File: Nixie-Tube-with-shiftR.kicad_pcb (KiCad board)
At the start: 2 copper layers, 37 x 44 mm, 55 parts, among them J1 Conn_01x06_Male, J2 Conn_01x01_Female, J3 Conn_01x06_Female, J4 Conn_01x01_Male, Q1 MMBTA42LT1, Q10 MMBTA42LT1, Q11 AO3400, Q12 AO3400, Q13 AO3400, Q14 MMBTA42LT1, Q15 MMBTA42LT1, Q2 MMBTA42LT1, Q3 MMBTA42LT1, Q4 MMBTA42LT1, Q5 MMBTA42LT1, Q6 MMBTA42LT1, Q7 MMBTA42LT1, Q8 MMBTA42LT1, Q9 MMBTA42LT1, U1 74HC595D, U2 nixie-tube, U3 74HC595D, U4 ams1117-5.0

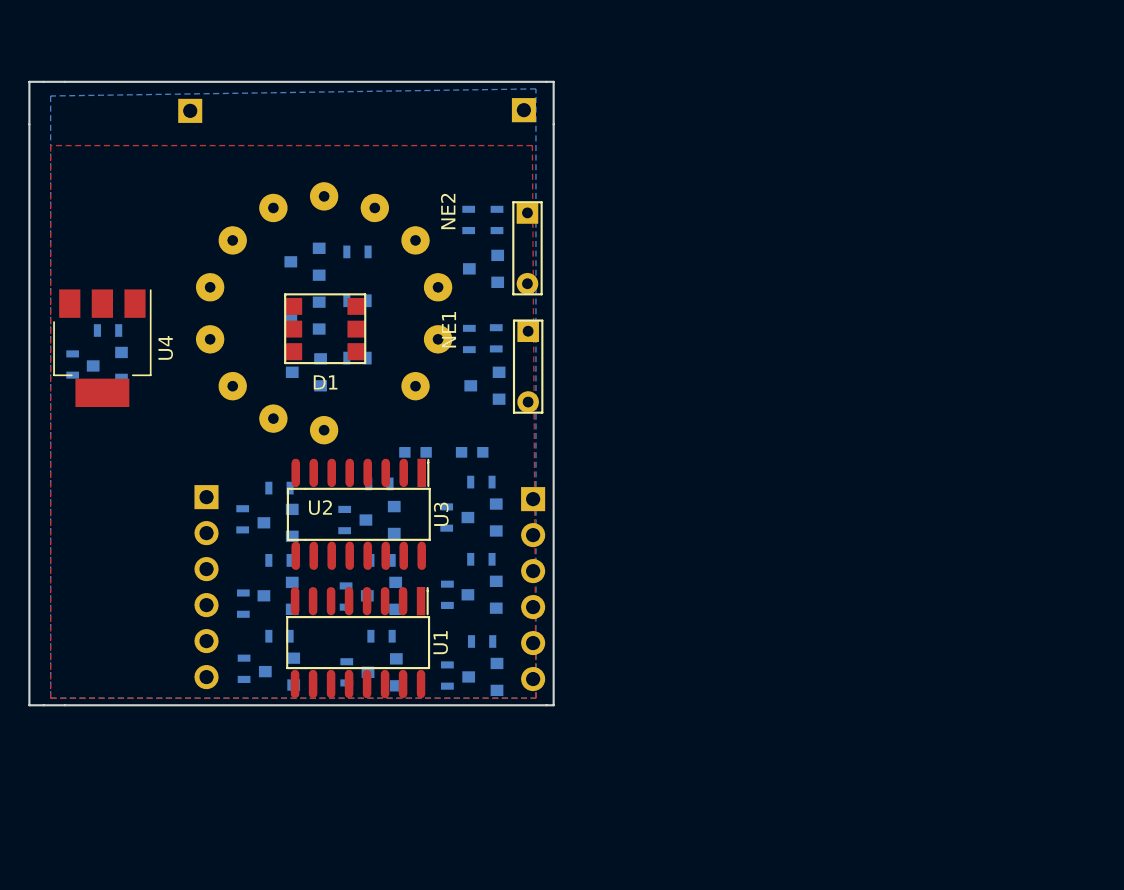
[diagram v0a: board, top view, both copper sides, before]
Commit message: finalized position, briefly routed
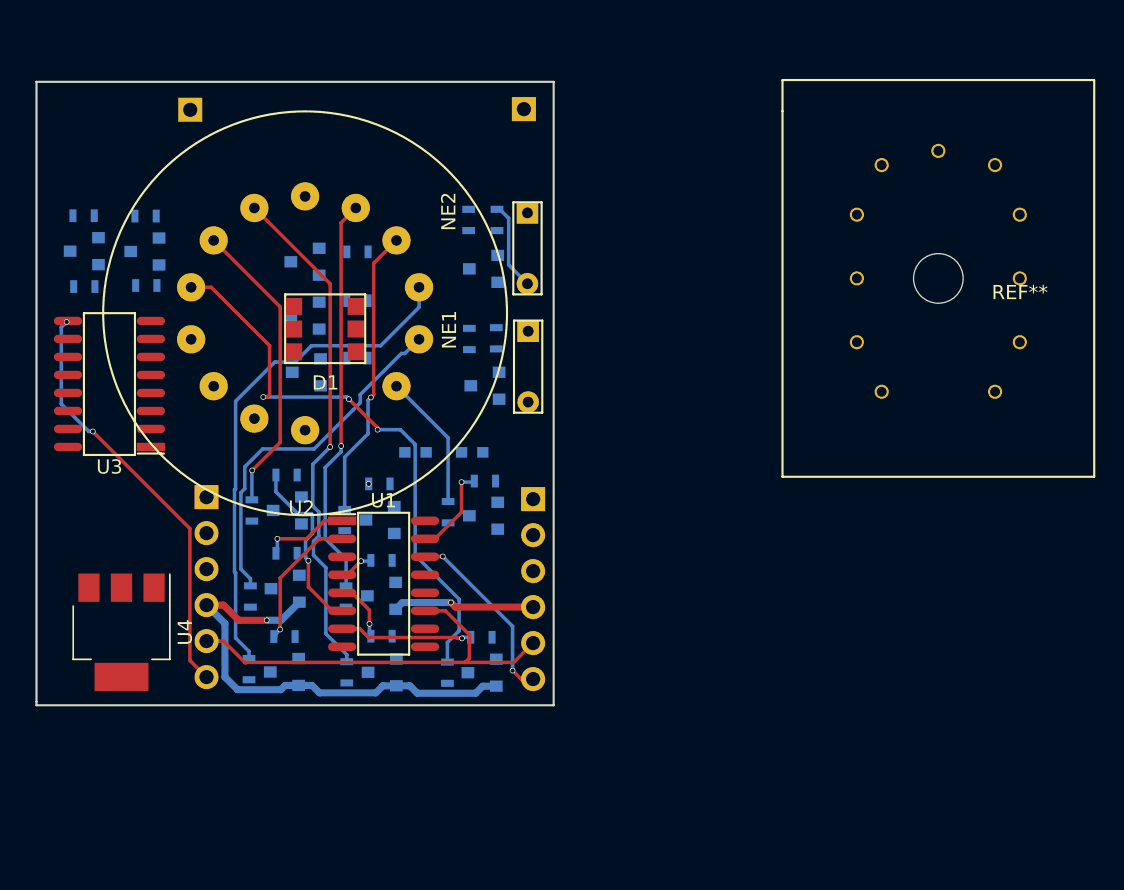
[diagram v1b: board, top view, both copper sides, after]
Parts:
- added REF**: qs27-1, nixie-tube-fp:qs27-1, F.Cu at (215.7, 57.9)
- moved Q3 41.2 mm to (155.4, 56.0)
- moved R16 41.2 mm to (155.3, 53.5)
- moved R2 37.6 mm to (155.4, 58.5), turned to 180 degrees
- moved U4 20.1 mm to (158.0, 82.8)
- moved U3 19.9 mm to (157.2, 65.3), turned to 180 degrees
- moved Q9 14.5 mm to (183.6, 74.6)
- moved R10 14.5 mm to (181.1, 74.4)
- moved R22 14.5 mm to (183.7, 72.2)
- moved Q8 13.8 mm to (169.7, 74.2)
- moved R21 13.8 mm to (169.7, 71.8)
- moved R4 13.8 mm to (167.2, 74.2), turned to 270 degrees
- moved Q1 8.50 mm to (159.7, 56.0)
- moved R14 8.50 mm to (159.7, 53.5)
- moved R1 7.62 mm to (159.8, 58.4), turned to 180 degrees
- moved Q6 5.50 mm to (183.4, 85.7)
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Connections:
- R11 pad 1: +9V -> +5V
- R12 pad 1: +9V -> +5V
- R13 pad 1: +9V -> +5V
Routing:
- net GND: track 0.00 -> 43.7 mm, vias 0 -> 2
- net Net-(R3-Pad1): track 0.00 -> 40.4 mm, vias 0 -> 3
- net Net-(R5-Pad1): track 0.00 -> 36.0 mm, vias 0 -> 1
- net Net-(R8-Pad1): track 0.00 -> 35.7 mm
- net /SCK: track 0.00 -> 30.2 mm
- net /MOSI-OUT: track 0.00 -> 29.7 mm, vias 0 -> 2
- net Net-(R6-Pad1): track 0.00 -> 28.2 mm, vias 0 -> 1
- net Net-(R9-Pad1): track 0.00 -> 25.2 mm
- net Net-(R4-Pad1): track 0.00 -> 21.1 mm, vias 0 -> 1
- net Net-(R7-Pad1): track 0.00 -> 20.5 mm, vias 0 -> 1
- net /MOSI: track 0.00 -> 13.0 mm, vias 0 -> 2
- net /s6: track 0.00 -> 12.9 mm, vias 0 -> 1
- net /s2: track 0.00 -> 9.75 mm, vias 0 -> 1
- net Net-(R10-Pad1): track 0.00 -> 9.65 mm
- net /s7: track 0.00 -> 9.39 mm, vias 0 -> 1
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- removed copper zone on F.Cu, net +9V
- removed copper zone on B.Cu, net GND
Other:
- board size 37 x 44 mm -> 36.5 x 44 mm

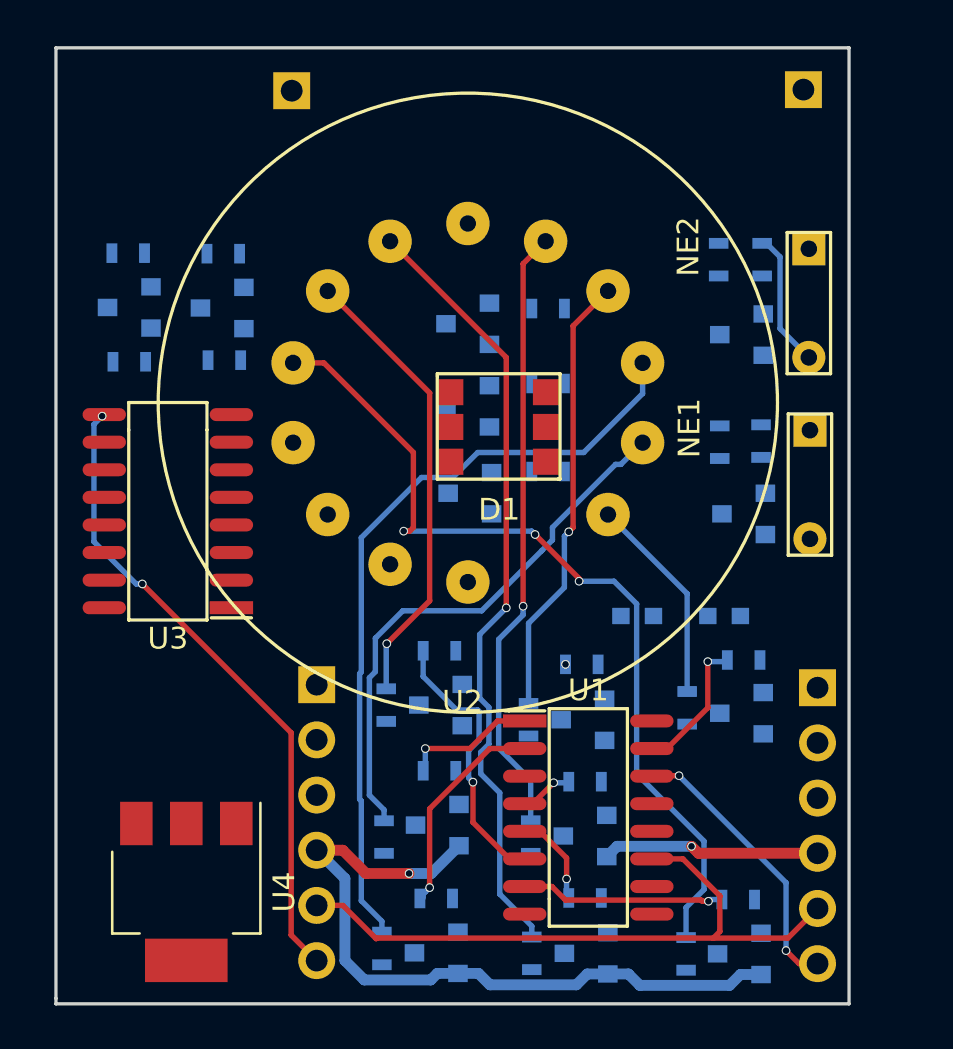
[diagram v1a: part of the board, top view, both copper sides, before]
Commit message: align the components
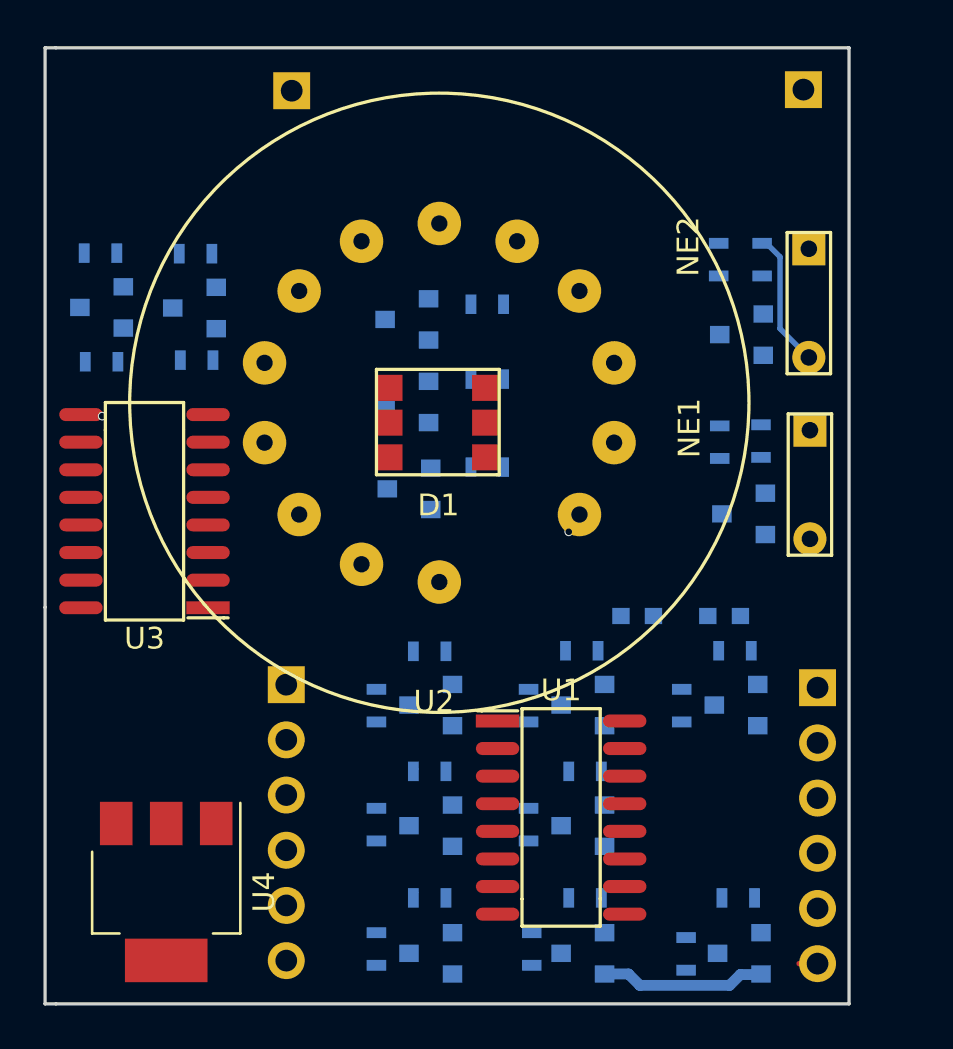
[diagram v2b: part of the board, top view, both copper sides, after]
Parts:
- moved Q11 2.81 mm to (168.2, 64.3)
- moved R11 2.81 mm to (171.8, 63.3)
- moved R12 2.81 mm to (171.8, 59.2)
- moved R13 2.81 mm to (171.8, 55.8)
- moved D1 2.81 mm to (169.7, 61.2)
- moved Q12 2.81 mm to (168.2, 60.3)
- moved Q13 2.81 mm to (168.2, 56.5)
- moved J1 1.40 mm to (162.6, 73.3)
- moved U2 1.31 mm to (169.6, 60.3)
- moved Q1 1.28 mm to (158.4, 56.0)
- moved Q3 1.28 mm to (154.1, 56.0)
- moved R1 1.28 mm to (158.5, 58.4)
- moved R2 1.28 mm to (154.1, 58.5)
- moved R14 1.27 mm to (158.4, 53.5)
- moved R16 1.27 mm to (154.1, 53.5)
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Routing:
- net Net-(R3-Pad1): track 40.4 -> 0.00 mm, vias 3 -> 0
- net GND: track 43.7 -> 7.47 mm, vias 2 -> 0
- net Net-(R5-Pad1): track 36.0 -> 0.00 mm, vias 1 -> 0
- net Net-(R8-Pad1): track 35.7 -> 0.00 mm
- net /SCK: track 30.2 -> 0.00 mm
- net /MOSI-OUT: track 29.7 -> 0.07 mm, vias 2 -> 1
- net Net-(R6-Pad1): track 28.2 -> 0.68 mm, vias 1 -> 0
- net Net-(R9-Pad1): track 25.2 -> 0.00 mm
- net Net-(R4-Pad1): track 21.1 -> 0.00 mm, vias 1 -> 0
- net Net-(R7-Pad1): track 20.5 -> 0.00 mm, vias 1 -> 0
- net /s6: track 12.9 -> 0.00 mm, vias 1 -> 0
- net /MOSI: track 13.0 -> 0.85 mm, vias 2 -> 0
- net /s2: track 9.75 -> 0.32 mm, vias 1 -> 0
- net /s7: track 9.39 -> 0.00 mm, vias 1 -> 0
- net Net-(R10-Pad1): track 9.65 -> 0.28 mm, vias 0 -> 1
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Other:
- board size 36.5 x 44 mm -> 37 x 44 mm

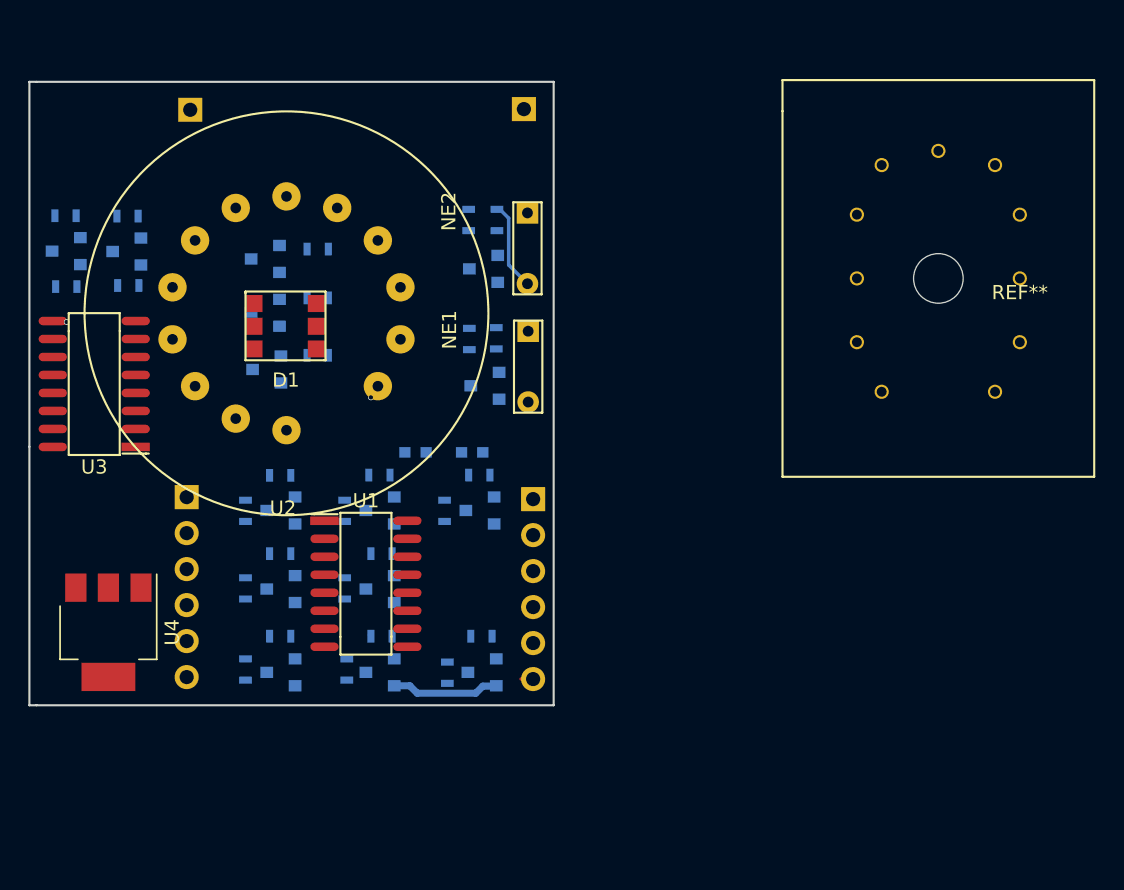
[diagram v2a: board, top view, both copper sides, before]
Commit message: finished routed all tracks
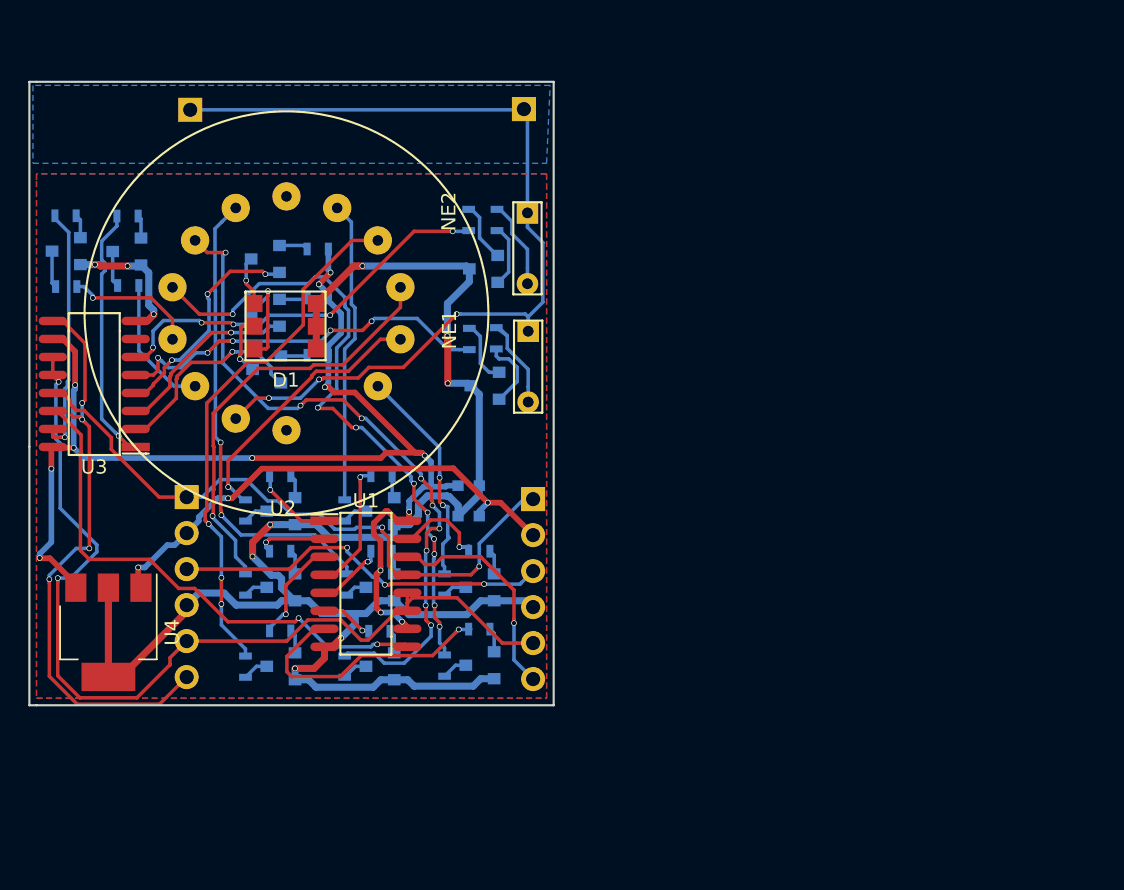
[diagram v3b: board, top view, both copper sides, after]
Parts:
- removed REF**: qs27-1, nixie-tube-fp:qs27-1
- moved Q4 13.0 mm to (169.2, 85.2)
- moved Q8 13.0 mm to (176.2, 85.2)
- moved R17 13.0 mm to (169.2, 82.8)
- moved R21 13.0 mm to (176.2, 82.8)
- moved R4 13.0 mm to (173.8, 85.3)
- moved R7 13.0 mm to (166.8, 85.3)
- moved Q10 6.00 mm to (176.2, 79.7)
- moved Q5 6.00 mm to (169.2, 79.7)
- moved R18 6.00 mm to (169.2, 77.1)
- moved R23 6.00 mm to (176.3, 77.1)
- moved R5 6.00 mm to (173.9, 79.5)
- moved R8 6.00 mm to (166.8, 79.5)
- moved Q2 5.50 mm to (176.2, 74.3)
- moved Q7 5.50 mm to (169.2, 74.3)
- moved R15 5.50 mm to (176.3, 71.8)
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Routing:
- net GND: track 7.47 -> 133.3 mm, vias 0 -> 10
- net +5V: track 0.00 -> 87.3 mm, vias 0 -> 13
- net /SCK: track 0.00 -> 67.1 mm, vias 0 -> 2
- net Net-(J2-Pad1): track 0.00 -> 64.0 mm, vias 0 -> 3
- net Net-(R4-Pad1): track 0.00 -> 48.3 mm, vias 0 -> 9
- net Net-(R3-Pad1): track 0.00 -> 45.8 mm, vias 0 -> 9
- net Net-(J1-Pad1): track 0.00 -> 45.5 mm, vias 0 -> 2
- net /MOSI-OUT: track 0.07 -> 40.7 mm, vias 1 -> 4
- net Net-(R7-Pad1): track 0.00 -> 37.4 mm, vias 0 -> 3
- net Net-(U1-Pad9): track 0.00 -> 37.1 mm, vias 0 -> 2
- net +9V: track 0.00 -> 35.6 mm, vias 0 -> 3
- net Net-(R5-Pad1): track 0.00 -> 33.3 mm, vias 0 -> 2
- net Net-(R8-Pad1): track 0.00 -> 30.1 mm, vias 0 -> 1
- net /DotD: track 0.00 -> 28.2 mm, vias 0 -> 5
- net /DotU: track 0.00 -> 27.3 mm, vias 0 -> 5
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- added copper zone on B.Cu, net GND
- added copper zone on F.Cu, net GND
- added copper zone on B.Cu, net Net-(J2-Pad1)
